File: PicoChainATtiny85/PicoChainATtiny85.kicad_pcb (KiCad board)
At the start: 2 copper layers, 60 x 34 mm, 11 parts, among them J1 RJ45, J2 RJ45, J3 Servo, U1 LM78M05, U2 PCA9615DP, U3 ATtiny85, U4 LM78M05

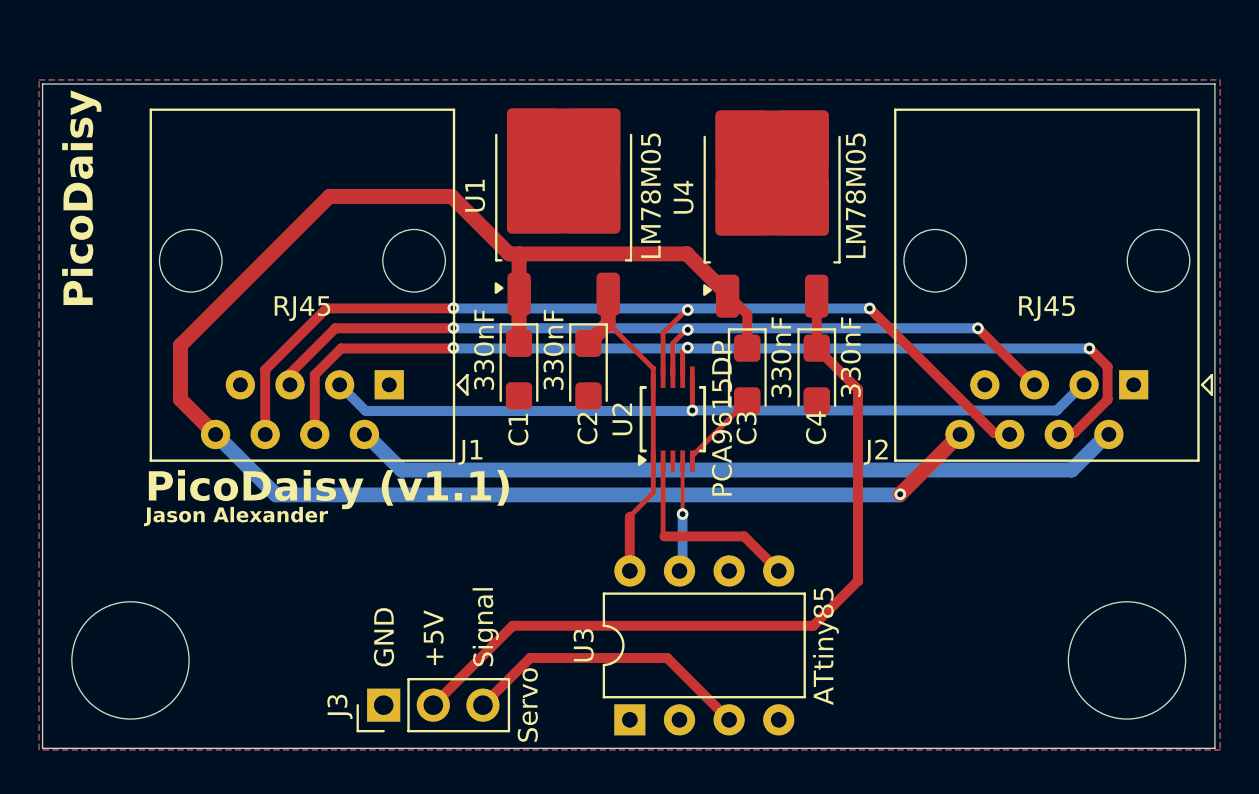
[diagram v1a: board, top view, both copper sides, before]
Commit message: Added open source hardware logo to PCBs
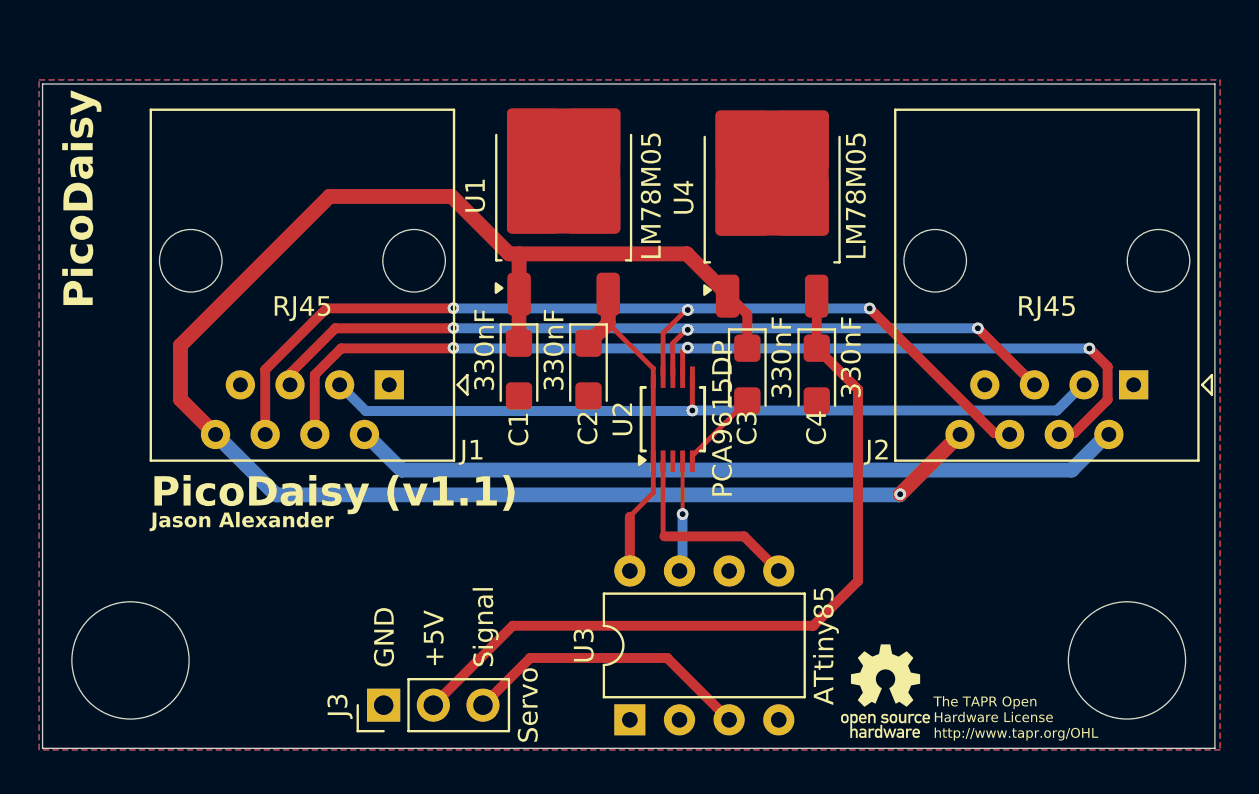
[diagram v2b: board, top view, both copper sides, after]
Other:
- board text added: "The TAPR Open Hardware License http://www.tapr.org/OHL"

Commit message: Made pass through power rails larger.
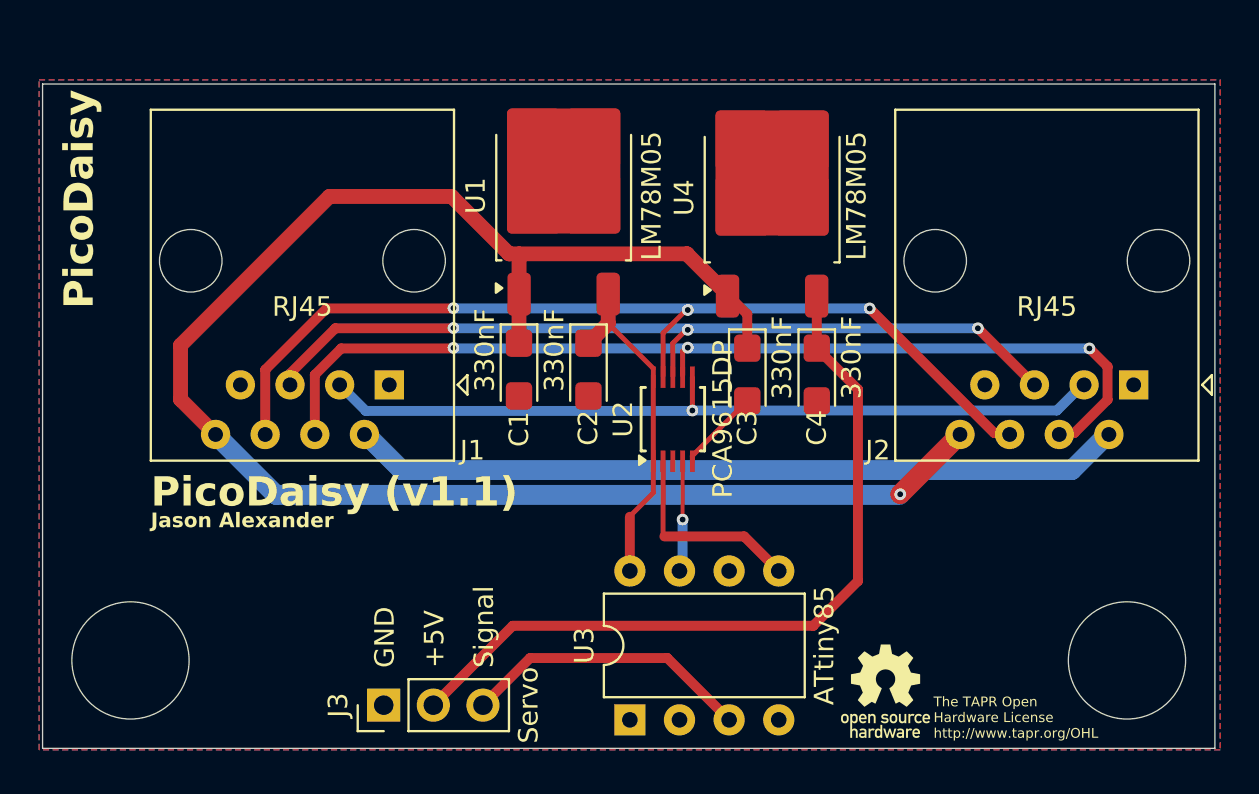
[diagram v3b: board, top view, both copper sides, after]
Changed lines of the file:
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@@
 		(start 143.89475 86.99575)
 		(end 146.9545 83.936)
-		(width 0.762)
+		(width 1.016)
 		(layer "F.Cu")
 		(net 4)
@@
 		(start 143.8635 87.027)
 		(end 111.9455 87.027)
-		(width 0.762)
+		(width 1.016)
 		(layer "B.Cu")
 		(net 4)
@@
 		(start 111.9455 87.027)
 		(end 108.8545 83.936)
-		(width 0.762)
+		(width 1.016)
 		(layer "B.Cu")
 		(net 4)
@@
 		(start 116.4745 83.856)
 		(end 118.3755 85.757)
-		(width 0.762)
+		(width 1.016)
 		(layer "B.Cu")
 		(net 12)
@@
 		(start 118.3755 85.757)
 		(end 152.6735 85.757)
-		(width 0.762)
+		(width 1.016)
 		(layer "B.Cu")
 		(net 12)
@@
 		(start 152.6735 85.757)
 		(end 154.5745 83.856)
-		(width 0.762)
+		(width 1.016)
 		(layer "B.Cu")
 		(net 12)
 	)
 	(segment
-		(start 132.758 88.011)
+		(start 132.758 88.2904)
 		(end 132.758 85.304)
 		(width 0.2)
@@
 	)
 	(via
-		(at 132.758 88.011)
-		(size 0.6)
-		(drill 0.3)
-		(layers "F.Cu" "B.Cu")
+		(at 132.758 88.2904)
+		(size 0.6)
+		(drill 0.3)
+		(layers "F.Cu" "B.Cu")
+		(net 13)
+	)
+	(segment
+		(start 132.758 88.2904)
+		(end 132.758 90.762)
+		(width 0.508)
+		(layer "B.Cu")
 		(net 13)
 	)
@@
 		(width 0.508)
 		(layer "B.Cu")
-		(net 13)
-	)
-	(segment
-		(start 132.758 88.011)
-		(end 132.758 90.762)
-		(width 0.508)
-		(layer "B.Cu")
